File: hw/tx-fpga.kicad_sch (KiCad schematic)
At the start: 15 parts, among them U2402 ICE40UP5K-SG48ITR, Y2402 ECS-TXO-2016-33-400-TR

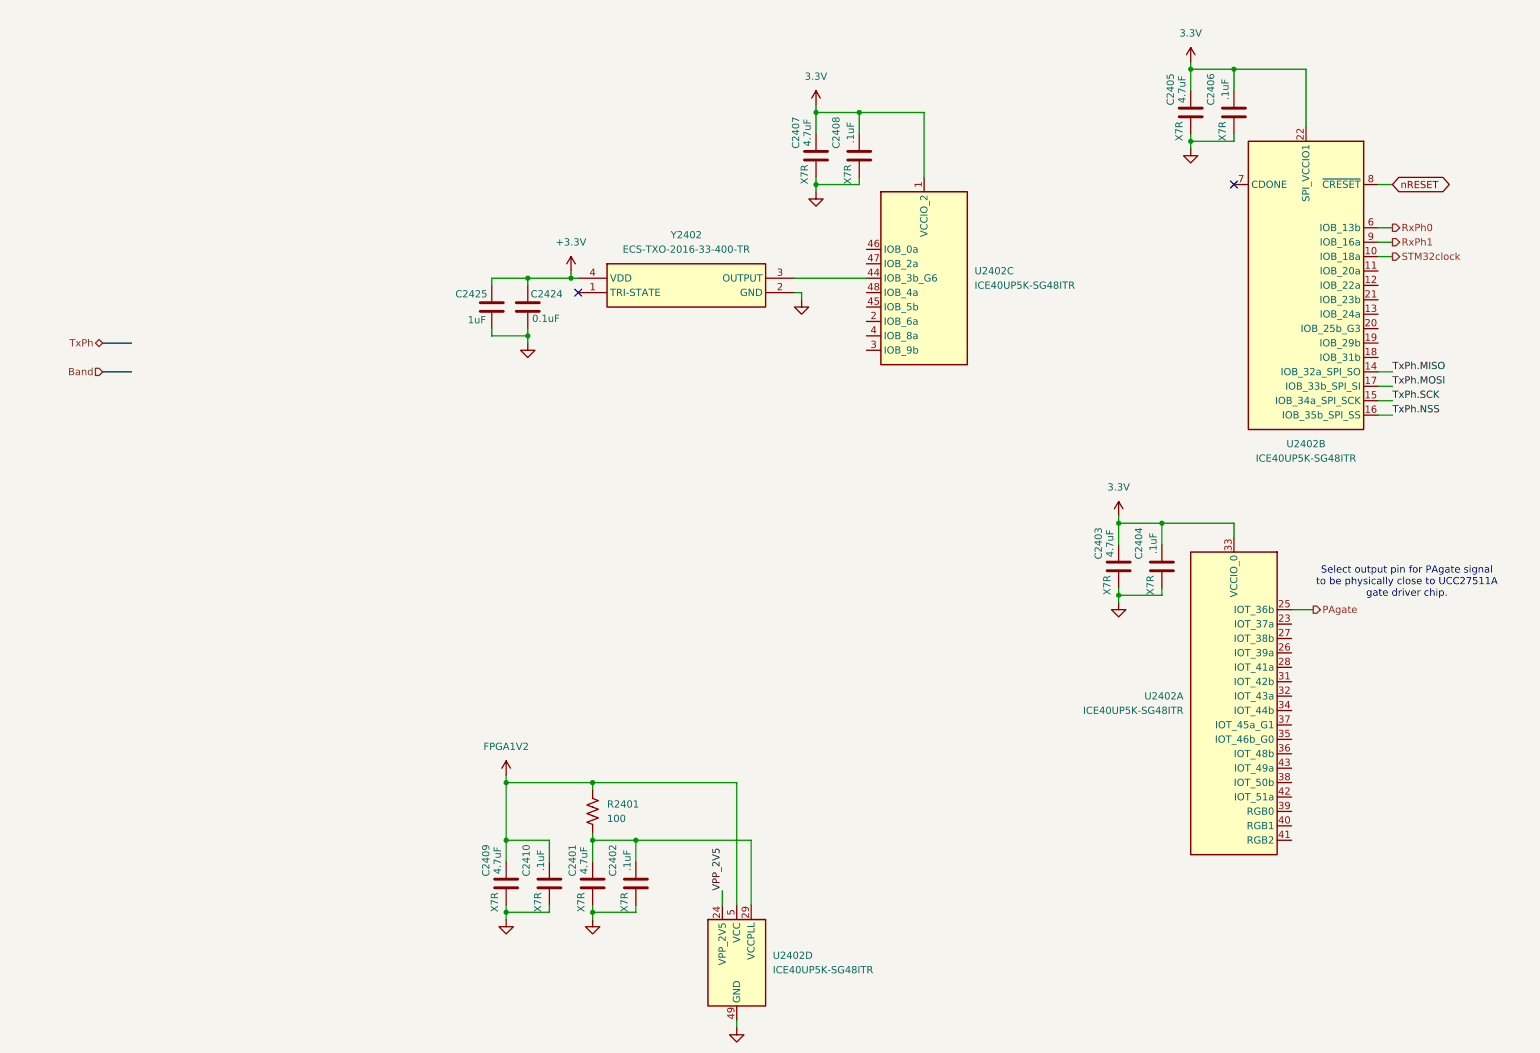
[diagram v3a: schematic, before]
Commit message: Starting FPGA power sequencing.
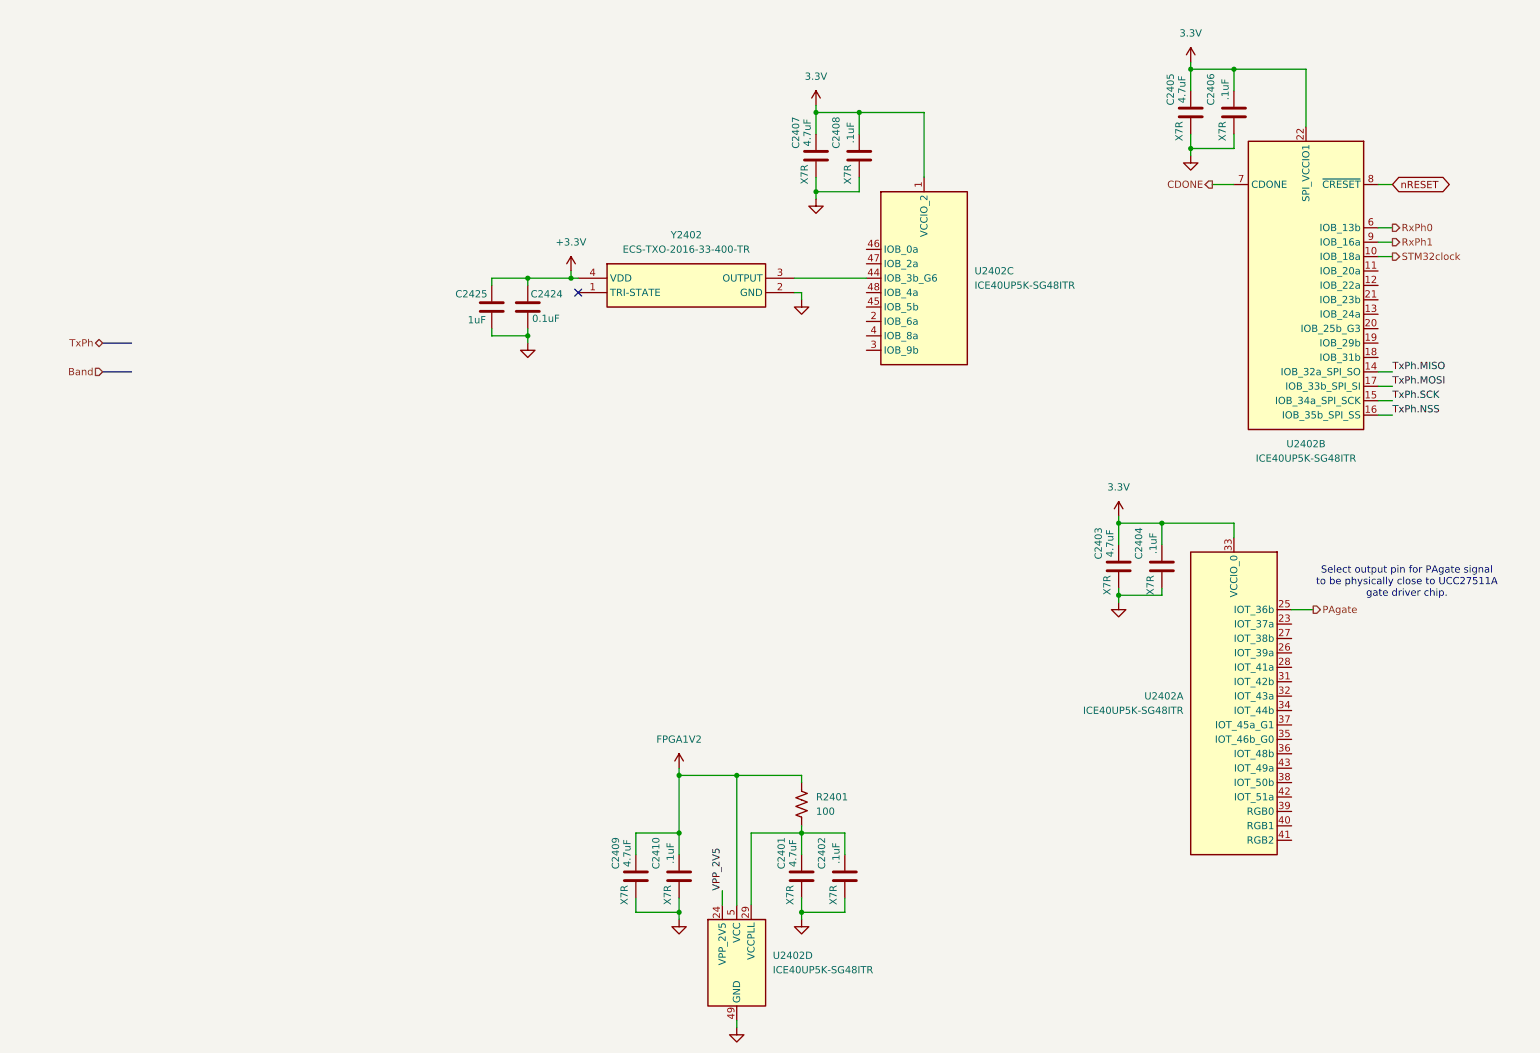
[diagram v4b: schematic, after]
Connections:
- net CDONE: now reaches U2402.7 (CDONE)
- no-connect marks 2 -> 1
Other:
- moved on the sheet: C2401, C2402, C2409, C2410, R2401

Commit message: Veer buck/boost schematic now seems done.
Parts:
- renumbered C2425 to C2401, C2424 to C2402, C2409 to C2403, C2410 to C2404, C2401 to C2405, C2407 to C2406, C2402 to C2407, C2403 to C2409, C2404 to C2410, C2405 to C2411, C2406 to C2412, U2402 to U2401, Y2402 to Y2401

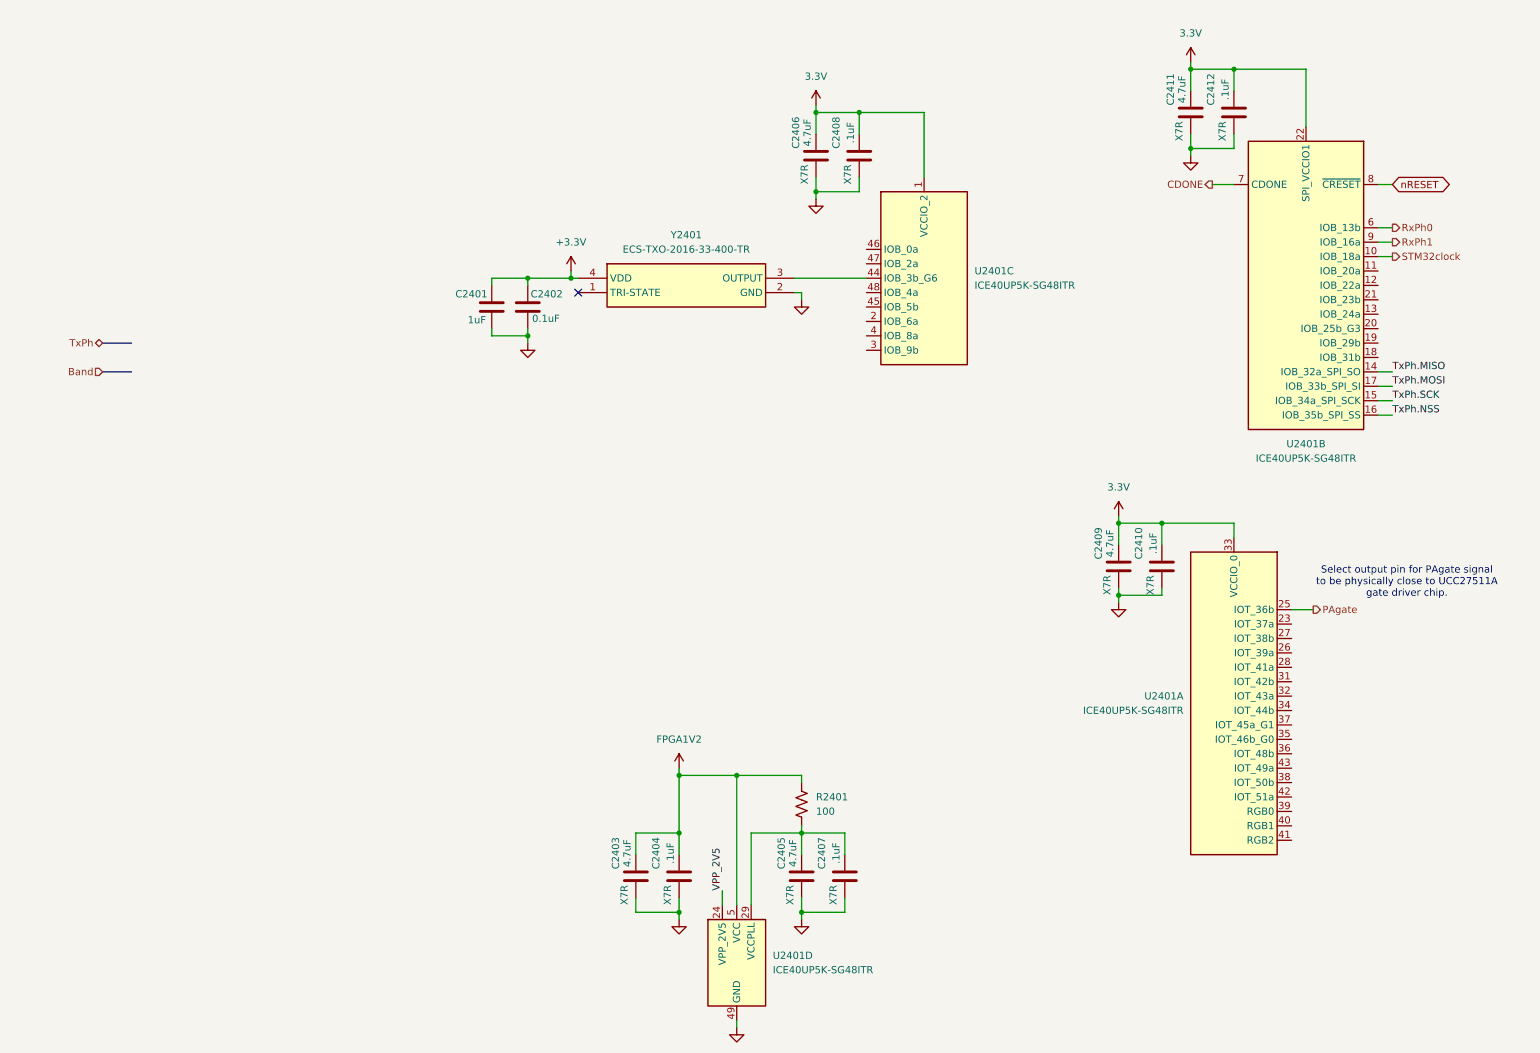
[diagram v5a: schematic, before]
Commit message: Embarking on a whole new arch for rx without BPFs and using a single digitally tuned tank plus three QSDs to accomplish image rejection in digital domain
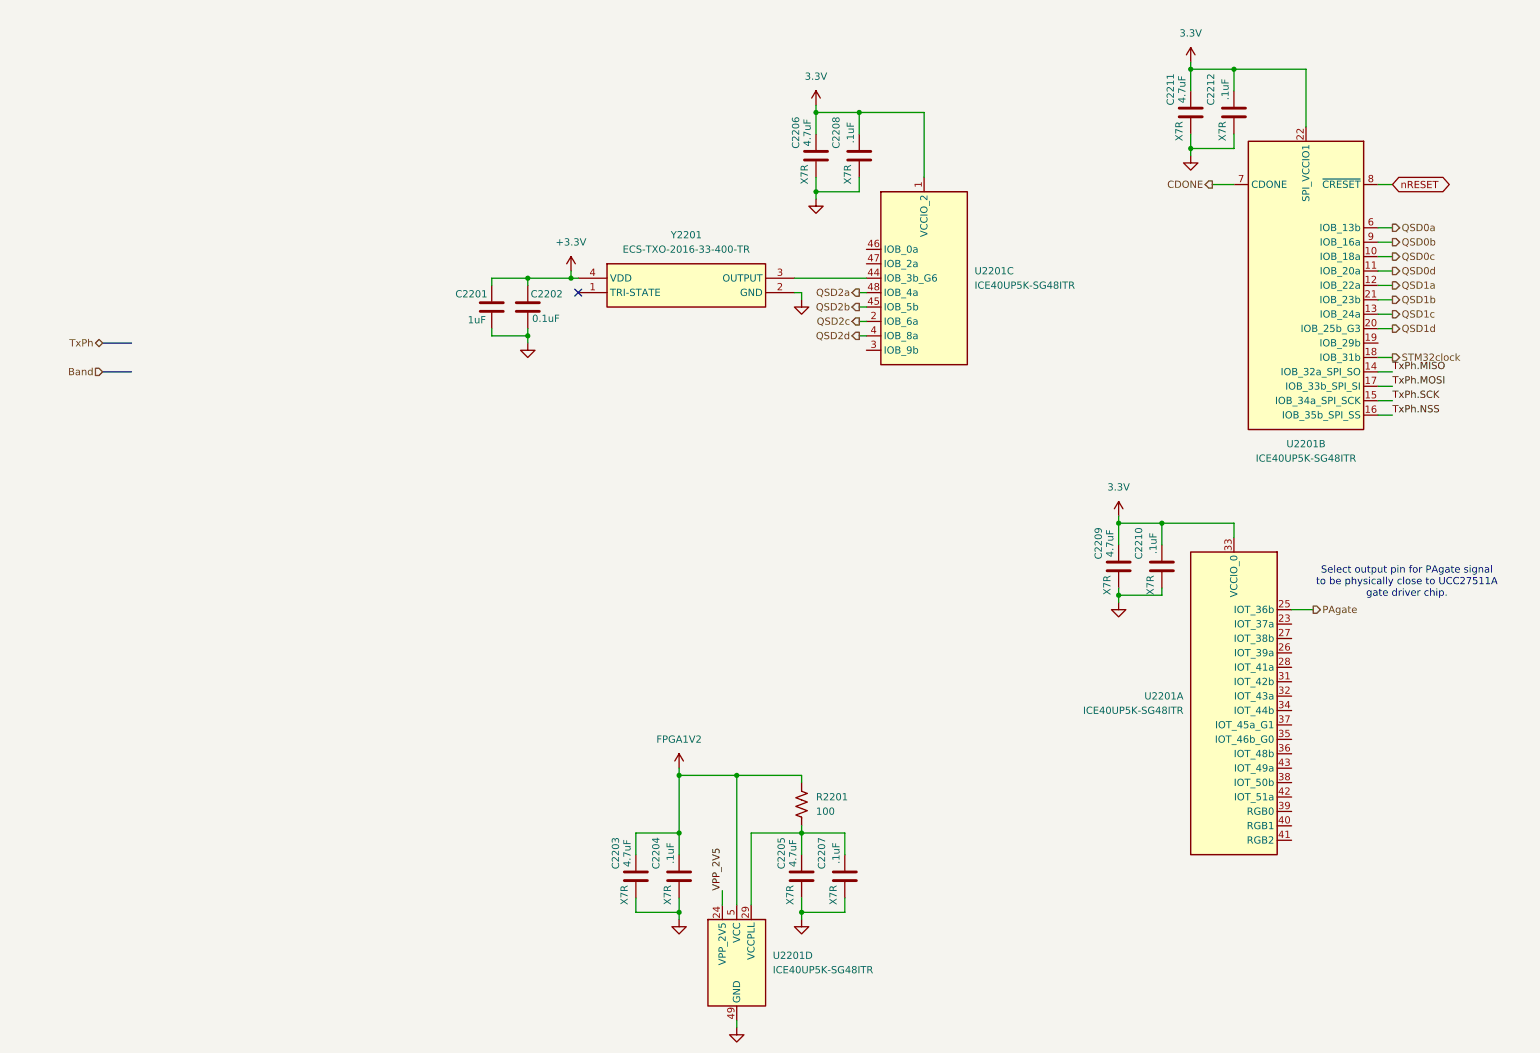
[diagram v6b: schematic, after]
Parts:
- C2201: renamed from C2401; footprint (none) -> Capacitor_SMD:C_0805_2012Metric
- C2202: renamed from C2402; footprint (none) -> Capacitor_SMD:C_0805_2012Metric
- C2203: renamed from C2403; footprint (none) -> Capacitor_SMD:C_0805_2012Metric
- C2204: renamed from C2404; footprint (none) -> Capacitor_SMD:C_0805_2012Metric
- C2205: renamed from C2405; footprint (none) -> Capacitor_SMD:C_0805_2012Metric
- C2206: renamed from C2406; footprint (none) -> Capacitor_SMD:C_0805_2012Metric
- C2207: renamed from C2407; footprint (none) -> Capacitor_SMD:C_0805_2012Metric
- C2208: renamed from C2408; footprint (none) -> Capacitor_SMD:C_0805_2012Metric
- C2209: renamed from C2409; footprint (none) -> Capacitor_SMD:C_0805_2012Metric
- C2210: renamed from C2410; footprint (none) -> Capacitor_SMD:C_0805_2012Metric
- C2211: renamed from C2411; footprint (none) -> Capacitor_SMD:C_0805_2012Metric
- C2212: renamed from C2412; footprint (none) -> Capacitor_SMD:C_0805_2012Metric
- Y2201: renamed from Y2401; footprint ECSTXO201633400TR -> (none)
- renumbered R2401 to R2201, U2401 to U2201
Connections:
- net STM32clock: now also U2201.18 (IOB_31b); no longer U2201.10 (IOB_18a)
- net QSD2c: now reaches U2201.2 (IOB_6a)
- net QSD2d: now reaches U2201.4 (IOB_8a)
- net QSD2b: now reaches U2201.45 (IOB_5b)
- net QSD2a: now reaches U2201.48 (IOB_4a)
- net QSD0d: now reaches U2201.11 (IOB_20a)
- net QSD1a: now reaches U2201.12 (IOB_22a)
- net QSD1c: now reaches U2201.13 (IOB_24a)
- net QSD1d: now reaches U2201.20 (IOB_25b_G3)
- net QSD1b: now reaches U2201.21 (IOB_23b)
- net RxPh0 renamed QSD0a
- net RxPh1 renamed QSD0b
- new net QSD0c: U2201.10 (IOB_18a)

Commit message: Starting to switch to new rx architecture
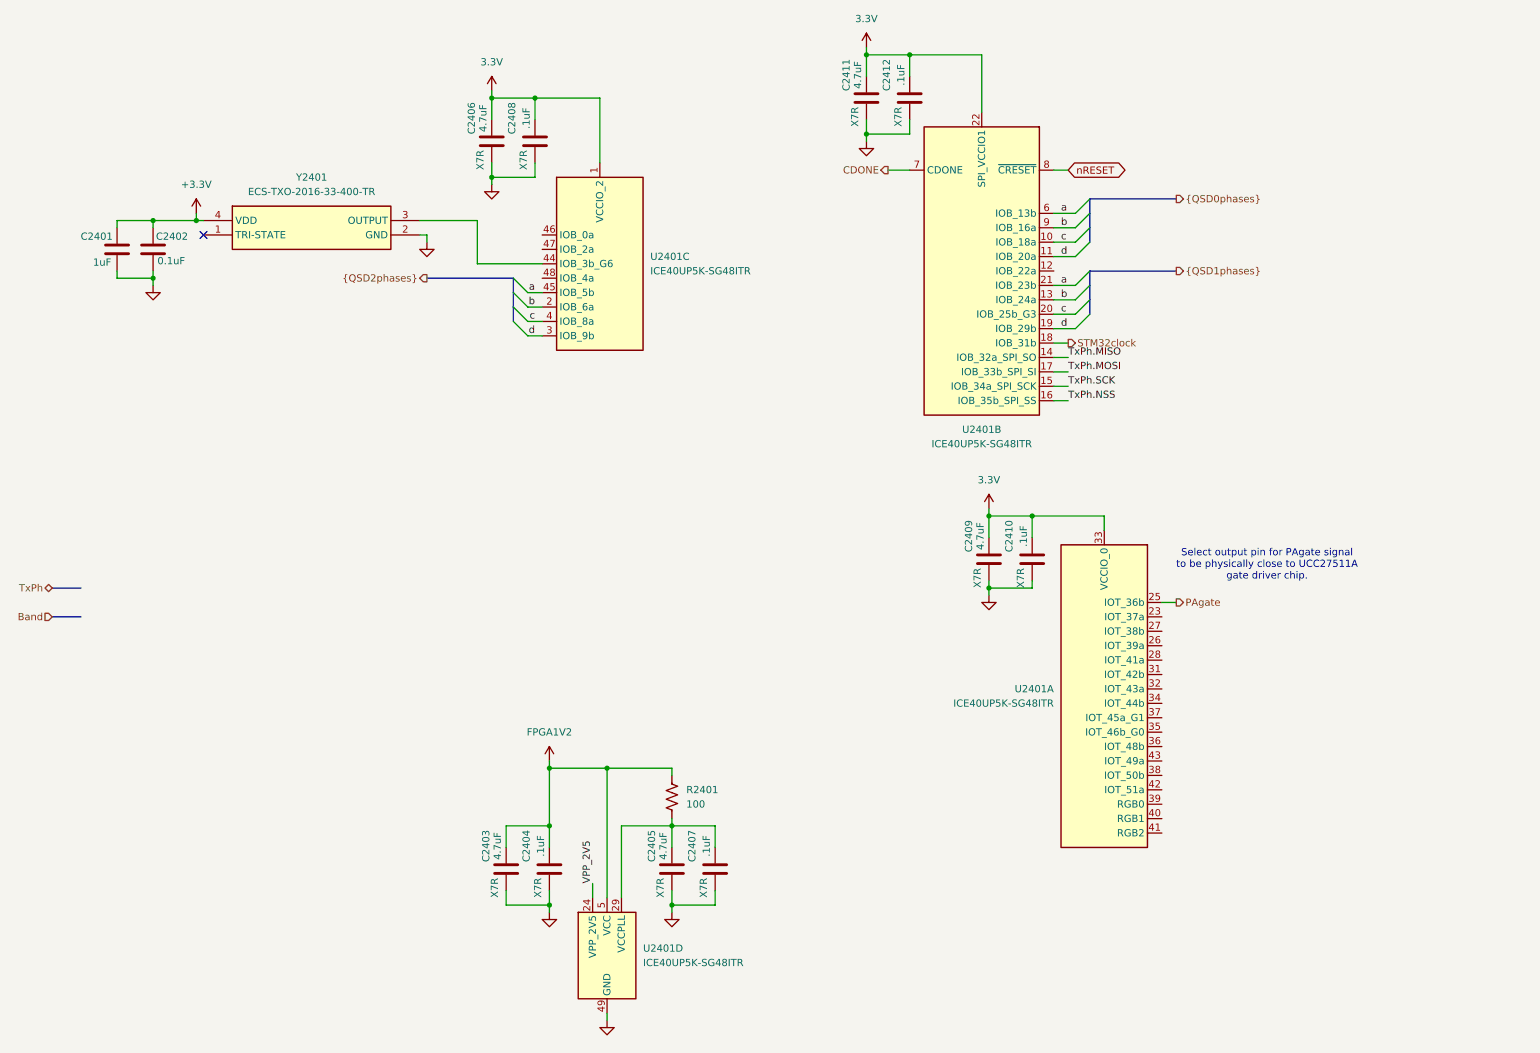
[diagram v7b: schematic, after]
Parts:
- renumbered C2201 to C2401, C2202 to C2402, C2203 to C2403, C2204 to C2404, C2205 to C2405, C2206 to C2406, C2207 to C2407, C2208 to C2408, C2209 to C2409, C2210 to C2410, C2211 to C2411, C2212 to C2412, R2201 to R2401, U2201 to U2401, Y2201 to Y2401
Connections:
- net QSD0d is gone; now on net d: U2401.11 (IOB_20a)
- net QSD1b is gone; now on net a: U2401.21 (IOB_23b)
- net QSD1c is gone; now on net b: U2401.13 (IOB_24a)
- net QSD1d is gone; now on net c: U2401.20 (IOB_25b_G3)
- net QSD2b is gone; now on net a: U2401.45 (IOB_5b)
- net QSD2c is gone; now on net b: U2401.2 (IOB_6a)
- net QSD2d is gone; now on net c: U2401.4 (IOB_8a)
- net d: now reaches U2401.3 (IOB_9b)
- net d: now also U2401.19 (IOB_29b)
- net QSD0a renamed a
- net QSD0b renamed b
- net QSD0c renamed c
- net QSD1a: no longer names the net of U2401.12 (IOB_22a)
- net QSD2a: no longer names the net of U2401.48 (IOB_4a)
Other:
- title: (none) -> FPGA
- moved on the sheet: C2401, C2402, C2403, C2404, C2405, C2406, C2407, C2408, C2409, C2410, C2411, C2412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
